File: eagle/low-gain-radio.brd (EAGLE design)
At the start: 99 x 98 mm, 135 parts, among them U1 MKW01Z128, U2 SKY65116, U3 W25Q80DV, U4 LP5907MFX-3.3, U6 LP5907MFX-3.3, U7 LD39200, U8 MAAL-010704, Y1 32MHz

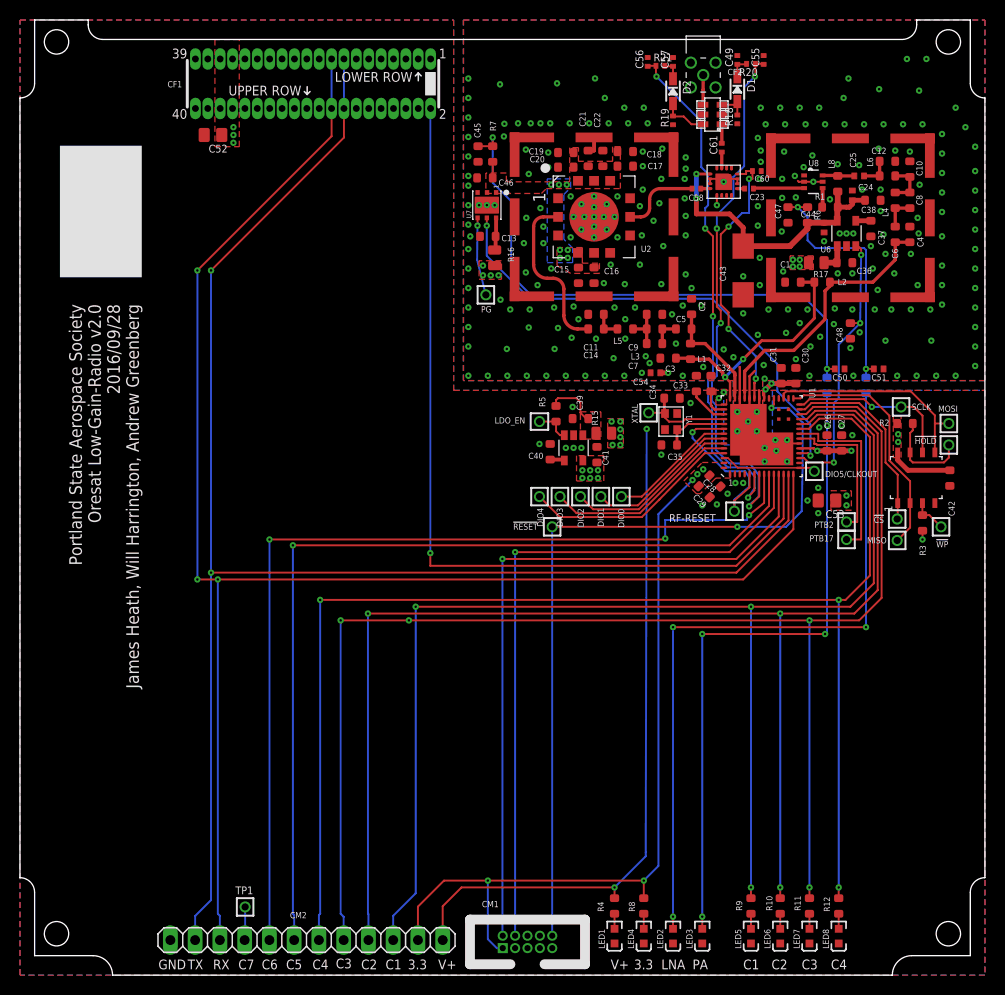
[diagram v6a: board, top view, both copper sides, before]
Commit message: Big cleanup of v2_0 board. Includes changes to packages for LDOs and switch and reflectometer, ground stapling, adding a RGB LED, new board outline from rev 0.4 structure drawings, etc. Ready for production, except for possible switch to 0402s.
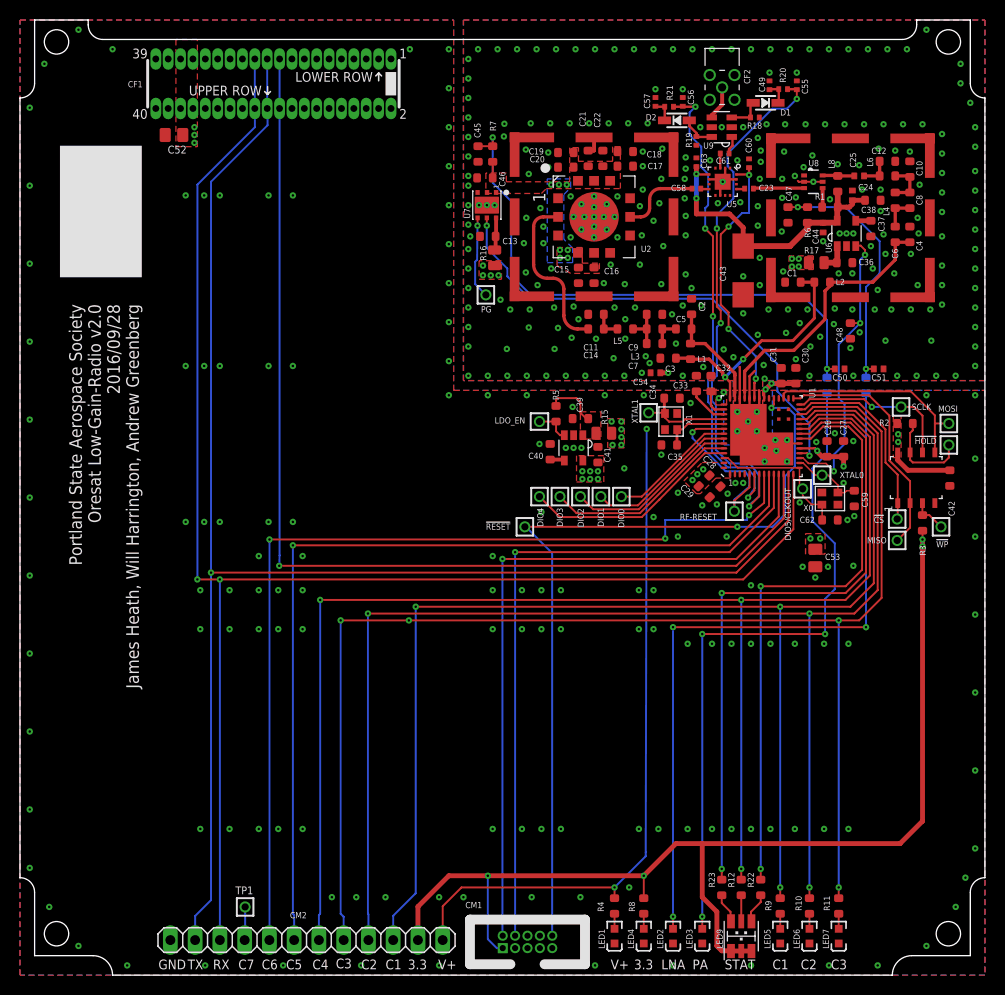
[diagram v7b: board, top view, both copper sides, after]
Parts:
- removed LED8: DNP/AMB, psas_c3_team05:LED-0603
- removed PTB17, PTB2: TEST-POINT, Tova:2MM-TEST-POINT
- removed U$22: BDCN-20-13+, low-gain-radio:FV1206-1
- removed U$49: RF3025, low-gain-radio:QFN-16_3MMX3MM
- added C59, C62: DNP, rcl_custom:.0603-B-NOSILK
- added C63: 100pF, low-gain-radio:.0402-C-NOSILK
- added LED9: SMLVN6RGB1W1, apdm:LED-3528
- added R22, R23: DNP/1k, rcl_custom:.0603-B-NOSILK@1
- added U5: RF3025, low-gain-radio:QFN-16_3MMX3MM
- added U9: BDCN-20-13+, low-gain-radio:FV1206-1
- added X0: DNP, microbuilder:CRYSTAL_2.5X2
- added XTAL0: TEST-POINT, Tova:2MM-TEST-POINT
- moved R12 10.2 mm to (74.0, 9.00)
- moved C53 6.02 mm to (81.6, 42.8), turned to 270 degrees
- moved C56 5.46 mm to (68.0, 89.6)
- moved C57 4.48 mm to (65.2, 89.6)
- moved R21 4.30 mm to (66.6, 89.1), turned to 180 degrees
- moved C55 4.28 mm to (79.7, 91.3)
- moved C49 4.20 mm to (76.9, 91.3)
- moved R20 4.20 mm to (78.3, 90.9)
- moved CF1 4.07 mm to (26.0, 91.5)
- moved C52 4.00 mm to (15.8, 86.2)
- moved D1 3.22 mm to (76.5, 89.5), turned to 180 degrees
- moved R19 3.19 mm to (69.4, 85.6)
- moved D2 3.03 mm to (67.4, 87.7), turned to 0 degrees
- moved LED5 3.00 mm to (78.0, 4.00)
- moved LED6 3.00 mm to (81.0, 4.00)
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- renumbered XTAL to XTAL1, Y1 to X1
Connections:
- removed net DIO5/CLKOUT: DIO5/CLKOUT.1, U1.15, U1.54
- new net EXTAL0: C62.2, DIO5/CLKOUT.1, U1.15, U1.54, X0.1
- new net N$11: LED9.6, R23.1
- new net N$26: LED9.5, R12.1
- new net XTAL0: C59.2, U1.16, X0.3, XTAL0.1
- net 3.3V: now also LED9.1, LED9.2, LED9.3
- net DC_OUT: now also U9.4; no longer U$22.OUT
- net FWD: now also U9.6; no longer U$22.FWD
- net GND: now also C59.1, C62.1; no longer LED8.K
- net LNA_IN: now also U5.13; no longer U$49.RF2
- net N$23: now also LED9.4, R22.1; no longer LED8.A, R12.1
- net PA_IN: now also U5.8; no longer U$49.RF1
- net PTA4/NMI_B: now also CF1.P$19, CF1.P$20; no longer CF1.P$2
- net PTB17: now also R23.2; no longer PTB17.1
- net PTB2: now also R22.2; no longer PTB2.1
- net REV: now also U9.3; no longer U$22.REV
- net RFC: now also U9.1; no longer U$22.IN
- net RF_GND: now also C63.1, U5.1, U5.10, U5.11, U5.12, U5.14, U5.15, U5.2, U5.4, U5.6, U5.7, U5.9, U5.PAD, U9.2, U9.5; no longer U$22.GND, U$22.GND2, U$49.GND, U$49.GND1, U$49.GND10, U$49.GND2, U$49.GND3, U$49.GND4, U$49.GND5, U$49.GND6, U$49.GND7, U$49.GND8, U$49.GND9, U$49.PADDLE
- net RXTX: now also U5.16; no longer U$49.VC
- net RXTX_OUT: now also U5.3; no longer U$49.RFC
- net UART0_RX: now also CF1.P$23, CF1.P$24; no longer CF1.P$17, CF1.P$18
- net UART0_TX: now also CF1.P$21, CF1.P$22; no longer CF1.P$15, CF1.P$16
- net VBIAS: now also C63.2, U5.5; no longer U$49.VDD
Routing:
- net PTB17: track 18.7 -> 66.9 mm, vias 0 -> 2
- net PTB2: track 15.5 -> 62.0 mm, vias 0 -> 2
- net 3.3V: track 97.8 -> 131.2 mm, vias 22 -> 23
- net PTA4/NMI_B: track 89.8 -> 110.5 mm, vias 2 -> 1
- net EXTAL0: track 0.00 -> 15.1 mm
- net DIO5/CLKOUT: track 9.84 -> 0.00 mm
- net XTAL0: track 0.00 -> 7.41 mm
- net VFWD: track 54.0 -> 50.1 mm
- net UART0_RX: track 165.1 -> 161.8 mm, vias 3 -> 2
- net N$11: track 0.00 -> 3.07 mm
- net UART0_TX: track 163.0 -> 159.9 mm, vias 2 -> 1
- net N$26: track 0.00 -> 2.67 mm
- net !RESET: track 82.3 -> 84.8 mm
- net LNA_EN: track 28.4 -> 30.8 mm
- net N$1: track 67.6 -> 69.5 mm
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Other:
- board text added: "STAT"

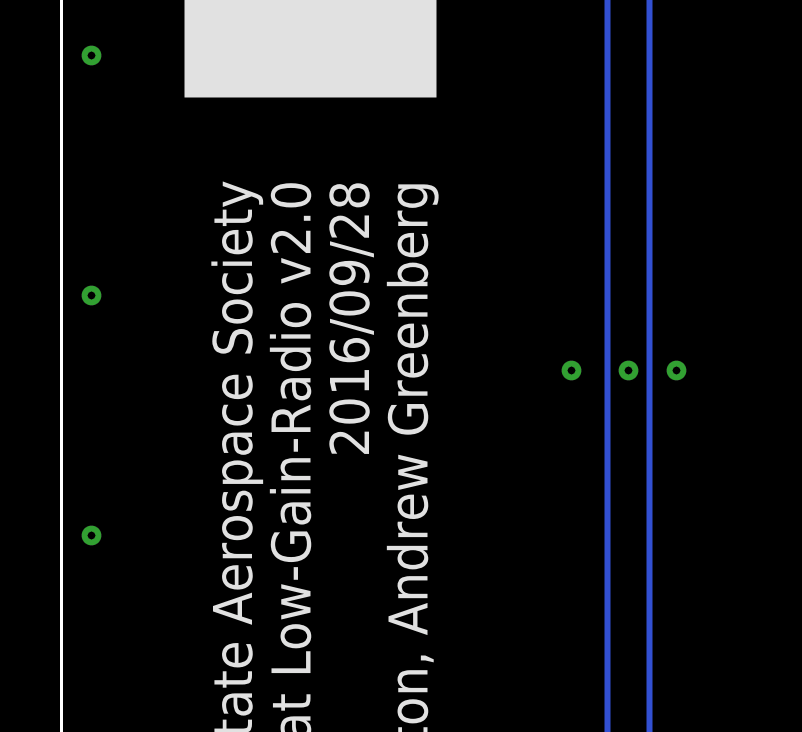
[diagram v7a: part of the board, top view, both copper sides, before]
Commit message: did a sanity check everything looks good, added some missing attributes to parts on the schematic and changed some text on the board layout
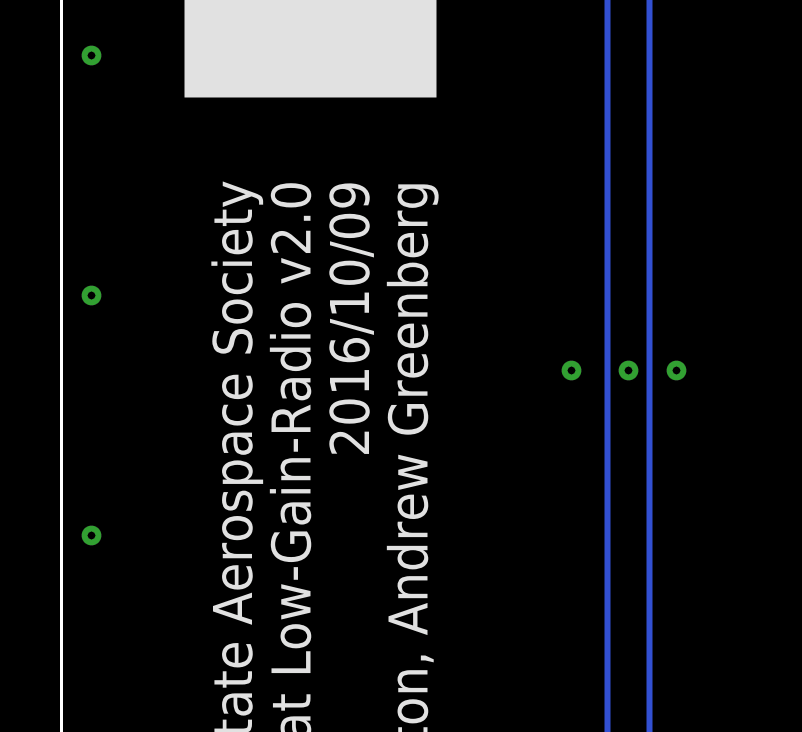
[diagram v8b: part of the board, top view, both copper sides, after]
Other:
- board text added: "Portland State Aerospace Society Oresat Low-Gain-Radio v2.0 2016/10/09 James Heath, Will Harrington, Andrew Greenberg"
- board text removed: "Portland State Aerospace Society Oresat Low-Gain-Radio v2.0 2016/09/28 James Heath, Will Harrington, Andrew Greenberg"
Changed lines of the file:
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@@
 <?xml version="1.0" encoding="utf-8"?>
 <!DOCTYPE eagle SYSTEM "eagle.dtd">
-<eagle version="7.5.0">
+<eagle version="7.3.0">
 <drawing>
 <settings>
@@
 <layer number="23" name="tOrigins" color="15" fill="1" visible="yes" active="yes"/>
 <layer number="24" name="bOrigins" color="15" fill="1" visible="yes" active="yes"/>
-<layer number="25" name="tNames" color="7" fill="1" visible="no" active="yes"/>
+<layer number="25" name="tNames" color="7" fill="1" visible="yes" active="yes"/>
 <layer number="26" name="bNames" color="7" fill="1" visible="no" active="yes"/>
 <layer number="27" name="tValues" color="7" fill="1" visible="no" active="yes"/>
@@
 <text x="5.05" y="68.85" size="1.3" layer="21" font="vector" ratio="15" rot="R270">Portland State Aerospace Society
 Oresat Low-Gain-Radio v2.0
-2016/09/28
+2016/10/09
 James Heath, Will Harrington, Andrew Greenberg</text>
 <wire x1="71.2" y1="81" x2="71.2" y2="81.4" width="0.1" layer="41"/>
@@
 <attribute name="NAME" x="63.7" y="74.2" size="0.635" layer="25" font="vector" ratio="20"/>
 <attribute name="VALUE" x="54.9" y="69.8" size="1.27" layer="27" font="vector" ratio="15"/>
+<attribute name="MFG" value="
+Skyworks Solutions Inc." x="58.9" y="77.8" size="1.778" layer="27" display="off"/>
+<attribute name="MPN" value="SKY65116-21" x="58.9" y="77.8" size="1.778" layer="27" display="off"/>
+<attribute name="DIST" value="Digi-Key Inc." x="58.9" y="77.8" size="1.778" layer="27" display="off"/>
+<attribute name="DPN" value="863-1072-1-ND" x="58.9" y="77.8" size="1.778" layer="27" display="off"/>
 </element>
 <element name="U8" library="psas_c3_team05" package="SOT-363" value="MAAL-010704" x="81.4" y="81.4" smashed="yes" rot="R270">
@@
 <attribute name="NAME" x="80.9" y="83" size="0.635" layer="25" font="vector" ratio="20"/>
 <attribute name="VALUE" x="82.4" y="79.4" size="0.635" layer="27" font="vector" ratio="20" rot="R270"/>
+<attribute name="MFG" value="M/A-Com Technology Solutions" x="81.4" y="81.4" size="1.778" layer="27" rot="R270" display="off"/>
+<attribute name="MPN" value="MAAL-010704-TR3000" x="81.4" y="81.4" size="1.778" layer="27" rot="R270" display="off"/>
+<attribute name="DIST" value="Digi-Key Inc." x="81.4" y="81.4" size="1.778" layer="27" rot="R270" display="off"/>
+<attribute name="DPN" value="1465-1261-1-ND" x="81.4" y="81.4" size="1.778" layer="27" rot="R270" display="off"/>
 </element>
 <element name="R13" library="rcl_custom" package=".0603-B-NOSILK@1" value="DNP/0" x="82.8" y="60.5" smashed="yes" rot="MR90">
@@
 <attribute name="VALUE" x="76.8" y="2.3" size="0.8" layer="27" font="vector" ratio="15" rot="R90"/>
 <attribute name="NAME" x="74" y="4" size="0.5" layer="33" ratio="15" rot="R270" align="center"/>
+<attribute name="MFG" value="Rohm Semiconductor" x="74" y="4" size="1.778" layer="27" rot="R90" display="off"/>
+<attribute name="MPN" value="SMLVN6RGB1W1" x="74" y="4" size="1.778" layer="27" rot="R90" display="off"/>
+<attribute name="DIST" value="Digi-Key Inc." x="74" y="4" size="1.778" layer="27" rot="R90" display="off"/>
+<attribute name="DPN" value="846-1187-1-ND" x="74" y="4" size="1.778" layer="27" rot="R90" display="off"/>
 </element>
 <element name="R12" library="rcl_custom" package=".0603-B-NOSILK@1" value="DNP/1k" x="74" y="9" smashed="yes" rot="R90">
@@
 <attribute name="NAME" x="72.5" y="78.8" size="0.635" layer="25" ratio="20"/>
 <attribute name="VALUE" x="72.1" y="79.4" size="0.635" layer="27" ratio="20" rot="R270"/>
+<attribute name="MFG" value="RFMD" x="72.1" y="81.4" size="1.778" layer="27" rot="R270" display="off"/>
+<attribute name="MPN" value="RF3025TR7" x="72.1" y="81.4" size="1.778" layer="27" rot="R270" display="off"/>
+<attribute name="DIST" value="Digi-Key Inc." x="72.1" y="81.4" size="1.778" layer="27" rot="R270" display="off"/>
+<attribute name="DPN" value="689-1087-1-ND" x="72.1" y="81.4" size="1.778" layer="27" rot="R270" display="off"/>
 </element>
 <element name="C63" library="low-gain-radio" package=".0402-C-NOSILK" value="100pF" x="69.4" y="83.4" smashed="yes" rot="R270">
